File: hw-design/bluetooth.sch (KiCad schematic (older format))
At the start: 22 parts, among them U7 BlueNRG, U8 BALF-NRG-01D3, Y2 32kHz, Y3 16MHz

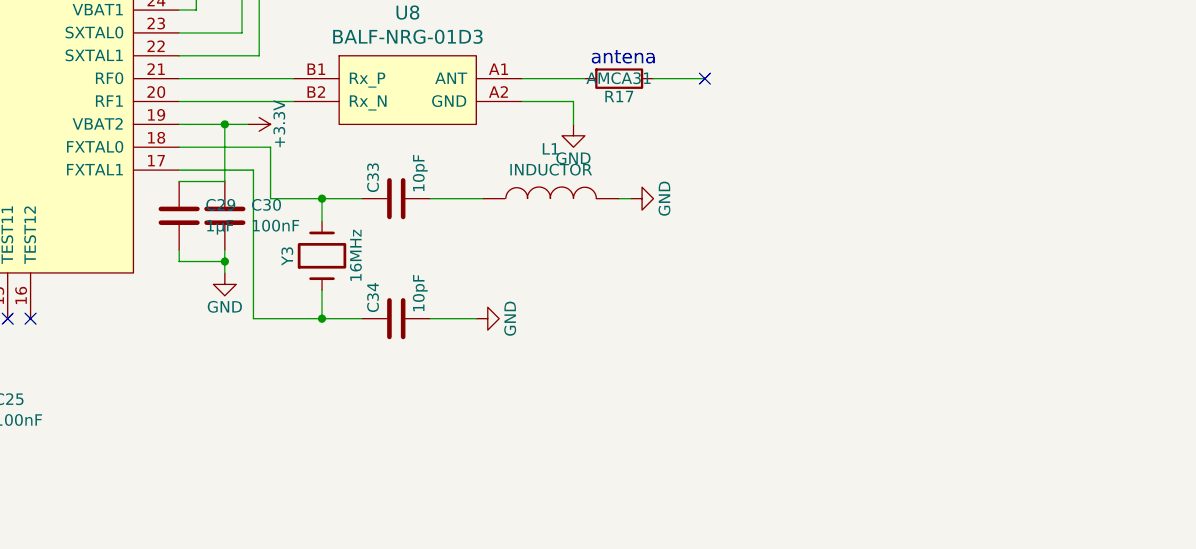
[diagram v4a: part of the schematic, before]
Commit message: BT turned of/on #define
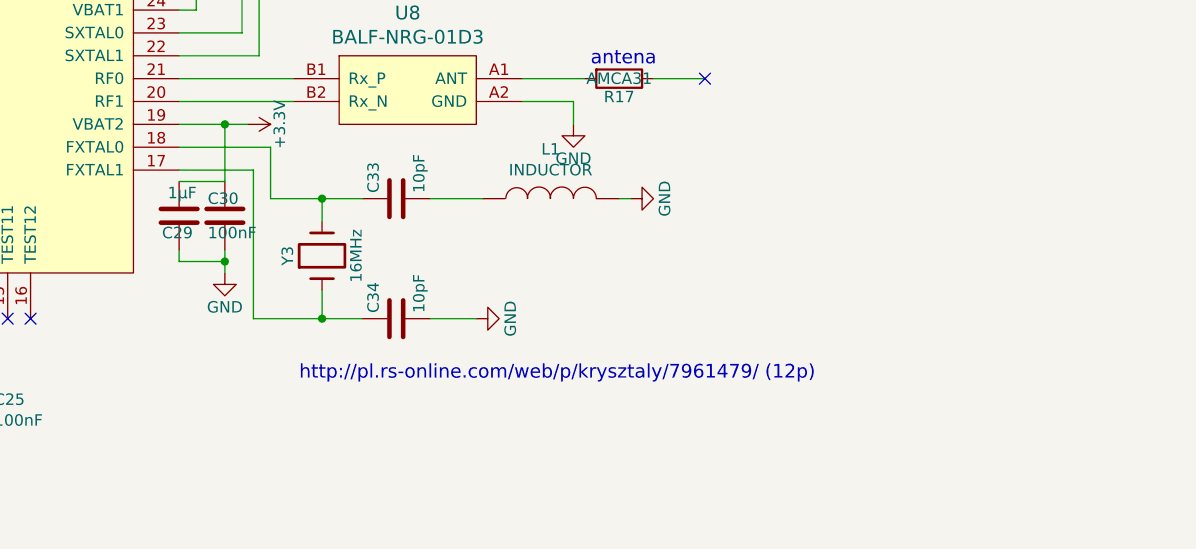
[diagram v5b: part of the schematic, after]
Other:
- note added: "http://pl.rs-online.com/web/p/krysztaly/7961479/ (12p)"
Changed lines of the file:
@@
 U 1 1 5725E354
 P 6600 4625
-F 0 "C30" H 6715 4671 50  0000 L CNN
-F 1 "100nF" H 6715 4580 50  0000 L CNN
+F 0 "C30" H 6525 4700 50  0000 L CNN
+F 1 "100nF" H 6525 4550 50  0000 L CNN
 F 2 "w_smd_cap:c_0603" H 6715 4534 50  0001 L CNN
 F 3 "" H 6600 4625 50  0000 C CNN
@@
 U 1 1 5725E361
 P 6400 4625
-F 0 "C29" H 6515 4671 50  0000 L CNN
-F 1 "1µF" H 6515 4580 50  0000 L CNN
+F 0 "C29" H 6325 4550 50  0000 L CNN
+F 1 "1µF" H 6350 4725 50  0000 L CNN
 F 2 "w_smd_cap:c_0603" H 6515 4534 50  0001 L CNN
 F 3 "" H 6400 4625 50  0000 C CNN
@@
 Text Notes 7250 2825 0    60   ~ 0
 http://www.ndk.com/en/products/search/crystal/1188854_1494.html\nhttp://pl.farnell.com/abracon/abs07-120-32-768khz-t/crystal-32-768khz-6pf-3-2-x-1/dp/2467864 (12.5pF)
+Text Notes 6925 5350 0    60   ~ 0
+http://pl.rs-online.com/web/p/krysztaly/7961479/ (12p)
 $EndSCHEMATC

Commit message: version 1.1 works.
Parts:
- C31, C32: value 6pF -> 22pF
- C33, C34: value 10pF -> 15pF
- Y2: Opis Kryształ 32kHz do timingu do nRF8001 -> Kryształ 32kHz do timingu do BLE
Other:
- note added: "http://www.ndk.com/en/products/search/crystal/1188854_1494.html\n"
- note removed: "http://pl.rs-online.com/web/p/krysztaly/7961479/ (12p)"
- note removed: "http://www.ndk.com/en/products/search/crystal/1188854_1494.html\nhttp://pl.farnell.com/abracon/abs07-120-32-768khz-t/crystal-32-768khz-6pf-3-2-x-1/dp/2467864 (12.5pF)"
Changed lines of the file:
@@
 F 1 "32kHz" H 7000 3100 50  0000 C CNN
 F 2 "iwasz:crystal_3.2_1.5" H 7000 3250 60  0001 C CNN
-F 3 "http://pl.farnell.com/abracon/abs07-120-32-768khz-t/crystal-32-768khz-6pf-3-2-x-1/dp/2467864" H 7000 3250 60  0001 C CNN
-F 4 "Kryształ 32kHz do timingu do nRF8001" H 7000 3250 60  0001 C CNN "Opis"
+F 3 "http://pl.farnell.com/abracon/abs07-32-768khz-t/crystal-32-768khz-12-5pf-smd/dp/2101347?MER=sy-me-pd-mi-alte" H 7000 3250 60  0001 C CNN
+F 4 "Kryształ 32kHz do timingu do BLE" H 7000 3250 60  0001 C CNN "Opis"
 	1    7000 3250
 	0    -1   -1   0
@@
 P 7325 3500
 F 0 "C32" H 7350 3600 50  0000 L CNN
-F 1 "6pF" H 7350 3400 50  0000 L CNN
+F 1 "22pF" H 7350 3400 50  0000 L CNN
 F 2 "w_smd_cap:c_0603" H 7363 3350 30  0001 C CNN
 F 3 "" H 7325 3500 60  0000 C CNN
@@
 P 7325 3025
 F 0 "C31" H 7350 3125 50  0000 L CNN
-F 1 "6pF" H 7350 2925 50  0000 L CNN
+F 1 "22pF" H 7350 2925 50  0000 L CNN
 F 2 "w_smd_cap:c_0603" H 7363 2875 30  0001 C CNN
 F 3 "" H 7325 3025 60  0000 C CNN
@@
 $EndComp
 $Comp
-L GND #PWR52
+L GND #PWR51
 U 1 1 5725E343
 P 8475 3250
-F 0 "#PWR52" H 8475 3000 50  0001 C CNN
+F 0 "#PWR51" H 8475 3000 50  0001 C CNN
 F 1 "GND" H 8475 3100 50  0000 C CNN
 F 2 "" H 8475 3250 60  0000 C CNN
@@
 F 1 "16MHz" H 7025 4650 50  0000 C CNN
 F 2 "Crystals:crystal_FA238-TSX3225" H 7025 4800 60  0001 C CNN
-F 3 "http://pl.farnell.com/abracon/abm8-16-000mhz-10-1-u-t/crystal-16mhz-10pf-3-2-x-2-5mm/dp/2467830" H 7025 4800 60  0001 C CNN
+F 3 "http://pl.farnell.com/epson/x1e0000210193-tsx-3225-16mhz-16pf/crystal-16mhz-16pf-3-2-x-2-5mm/dp/2471828" H 7025 4800 60  0001 C CNN
 F 4 "Kryształ 16MHz do radia do nRF8001" H 7025 4800 60  0001 C CNN "Opis"
 	1    7025 4800
@@
 P 7350 4550
 F 0 "C33" H 7375 4650 50  0000 L CNN
-F 1 "10pF" H 7375 4450 50  0000 L CNN
+F 1 "15pF" H 7375 4450 50  0000 L CNN
 F 2 "w_smd_cap:c_0603" H 7388 4400 30  0001 C CNN
 F 3 "" H 7350 4550 60  0000 C CNN
@@
 P 7350 5075
 F 0 "C34" H 7375 5175 50  0000 L CNN
-F 1 "10pF" H 7375 4975 50  0000 L CNN
+F 1 "15pF" H 7375 4975 50  0000 L CNN
 F 2 "w_smd_cap:c_0603" H 7388 4925 30  0001 C CNN
 F 3 "" H 7350 5075 60  0000 C CNN
@@
 	6400 4125 6900 4125
 $Comp
-L GND #PWR50
+L GND #PWR49
 U 1 1 5725E34A
 P 8125 4225
-F 0 "#PWR50" H 8125 3975 50  0001 C CNN
+F 0 "#PWR49" H 8125 3975 50  0001 C CNN
 F 1 "GND" H 8125 4075 50  0000 C CNN
 F 2 "" H 8125 4225 60  0000 C CNN
@@
 	8125 4125 8125 4225
 $Comp
-L GND #PWR49
+L GND #PWR48
 U 1 1 5725E34B
 P 7700 5075
-F 0 "#PWR49" H 7700 4825 50  0001 C CNN
+F 0 "#PWR48" H 7700 4825 50  0001 C CNN
 F 1 "GND" H 7700 4925 50  0000 C CNN
 F 2 "" H 7700 5075 60  0000 C CNN
@@
 $EndComp
 $Comp
-L GND #PWR51
+L GND #PWR50
 U 1 1 5725E34C
 P 8375 4550
-F 0 "#PWR51" H 8375 4300 50  0001 C CNN
+F 0 "#PWR50" H 8375 4300 50  0001 C CNN
 F 1 "GND" H 8375 4400 50  0000 C CNN
 F 2 "" H 8375 4550 60  0000 C CNN
@@
 	5475 5675 5475 5625
 $Comp
-L GND #PWR43
+L GND #PWR42
 U 1 1 5725E34F
 P 5350 5800
-F 0 "#PWR43" H 5350 5550 50  0001 C CNN
+F 0 "#PWR42" H 5350 5550 50  0001 C CNN
 F 1 "GND" H 5350 5650 50  0000 C CNN
 F 2 "" H 5350 5800 60  0000 C CNN
@@
 Connection ~ 5350 5250
 $Comp
-L GND #PWR41
+L GND #PWR40
 U 1 1 5725E350
 P 5050 5250
-F 0 "#PWR41" H 5050 5000 50  0001 C CNN
+F 0 "#PWR40" H 5050 5000 50  0001 C CNN
 F 1 "GND" H 5050 5100 50  0000 C CNN
 F 2 "" H 5050 5250 60  0000 C CNN
@@
 Connection ~ 5150 5125
 $Comp
-L GND #PWR39
+L GND #PWR38
 U 1 1 5725E351
 P 4300 4675
-F 0 "#PWR39" H 4300 4425 50  0001 C CNN
+F 0 "#PWR38" H 4300 4425 50  0001 C CNN
 F 1 "GND" H 4300 4525 50  0000 C CNN
 F 2 "" H 4300 4675 60  0000 C CNN
@@
 Connection ~ 4300 4550
 $Comp
-L +3.3V #PWR38
+L +3.3V #PWR37
 U 1 1 5725E353
 P 3950 4125
-F 0 "#PWR38" H 3950 3975 50  0001 C CNN
+F 0 "#PWR37" H 3950 3975 50  0001 C CNN
 F 1 "+3.3V" H 3950 4265 50  0000 C CNN
 F 2 "" H 3950 4125 60  0000 C CNN
@@
 $EndComp
 $Comp
-L +3.3V #PWR48
+L +3.3V #PWR47
 U 1 1 5725E355
 P 6700 4225
-F 0 "#PWR48" H 6700 4075 50  0001 C CNN
+F 0 "#PWR47" H 6700 4075 50  0001 C CNN
 F 1 "+3.3V" H 6700 4365 50  0000 C CNN
 F 2 "" H 6700 4225 60  0000 C CNN
@@
 Connection ~ 6600 4225
 $Comp
-L GND #PWR47
+L GND #PWR46
 U 1 1 5725E356
 P 6600 4875
-F 0 "#PWR47" H 6600 4625 50  0001 C CNN
+F 0 "#PWR46" H 6600 4625 50  0001 C CNN
 F 1 "GND" H 6600 4725 50  0000 C CNN
 F 2 "" H 6600 4875 60  0000 C CNN
@@
 	5750 3075 5750 2900
 $Comp
-L +3.3V #PWR46
+L +3.3V #PWR45
 U 1 1 5725E357
 P 6475 2100
-F 0 "#PWR46" H 6475 1950 50  0001 C CNN
+F 0 "#PWR45" H 6475 1950 50  0001 C CNN
 F 1 "+3.3V" H 6475 2240 50  0000 C CNN
 F 2 "" H 6475 2100 60  0000 C CNN
@@
 	6075 2300 6125 2300
 $Comp
-L GND #PWR45
+L GND #PWR44
 U 1 1 5725E35A
 P 6075 2075
-F 0 "#PWR45" H 6075 1825 50  0001 C CNN
+F 0 "#PWR44" H 6075 1825 50  0001 C CNN
 F 1 "GND" H 6075 1925 50  0000 C CNN
 F 2 "" H 6075 2075 60  0000 C CNN
@@
 $EndComp
 $Comp
-L GND #PWR42
+L GND #PWR41
 U 1 1 5725E35C
 P 5250 1975
-F 0 "#PWR42" H 5250 1725 50  0001 C CNN
+F 0 "#PWR41" H 5250 1725 50  0001 C CNN
 F 1 "GND" H 5250 1825 50  0000 C CNN
 F 2 "" H 5250 1975 60  0000 C CNN
@@
 Connection ~ 5950 2725
 $Comp
-L GND #PWR44
+L GND #PWR43
 U 1 1 5725E35F
 P 5950 3125
-F 0 "#PWR44" H 5950 2875 50  0001 C CNN
+F 0 "#PWR43" H 5950 2875 50  0001 C CNN
 F 1 "GND" H 5950 2975 50  0000 C CNN
 F 2 "" H 5950 3125 60  0000 C CNN
@@
 	3950 4550 4300 4550
 $Comp
-L GND #PWR40
+L GND #PWR39
 U 1 1 5725E362
 P 4750 3000
-F 0 "#PWR40" H 4750 2750 50  0001 C CNN
+F 0 "#PWR39" H 4750 2750 50  0001 C CNN
 F 1 "GND" H 4750 2850 50  0000 C CNN
 F 2 "" H 4750 3000 60  0000 C CNN
@@
 	8375 3250 8475 3250
 Text Notes 7250 2825 0    60   ~ 0
-http://www.ndk.com/en/products/search/crystal/1188854_1494.html\nhttp://pl.farnell.com/abracon/abs07-120-32-768khz-t/crystal-32-768khz-6pf-3-2-x-1/dp/2467864 (12.5pF)
-Text Notes 6925 5350 0    60   ~ 0
-http://pl.rs-online.com/web/p/krysztaly/7961479/ (12p)
+http://www.ndk.com/en/products/search/crystal/1188854_1494.html\n
 $EndSCHEMATC
